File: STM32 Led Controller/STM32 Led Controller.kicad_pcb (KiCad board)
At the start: 2 copper layers, 1 part, among them U1 STM32G0B0RETx

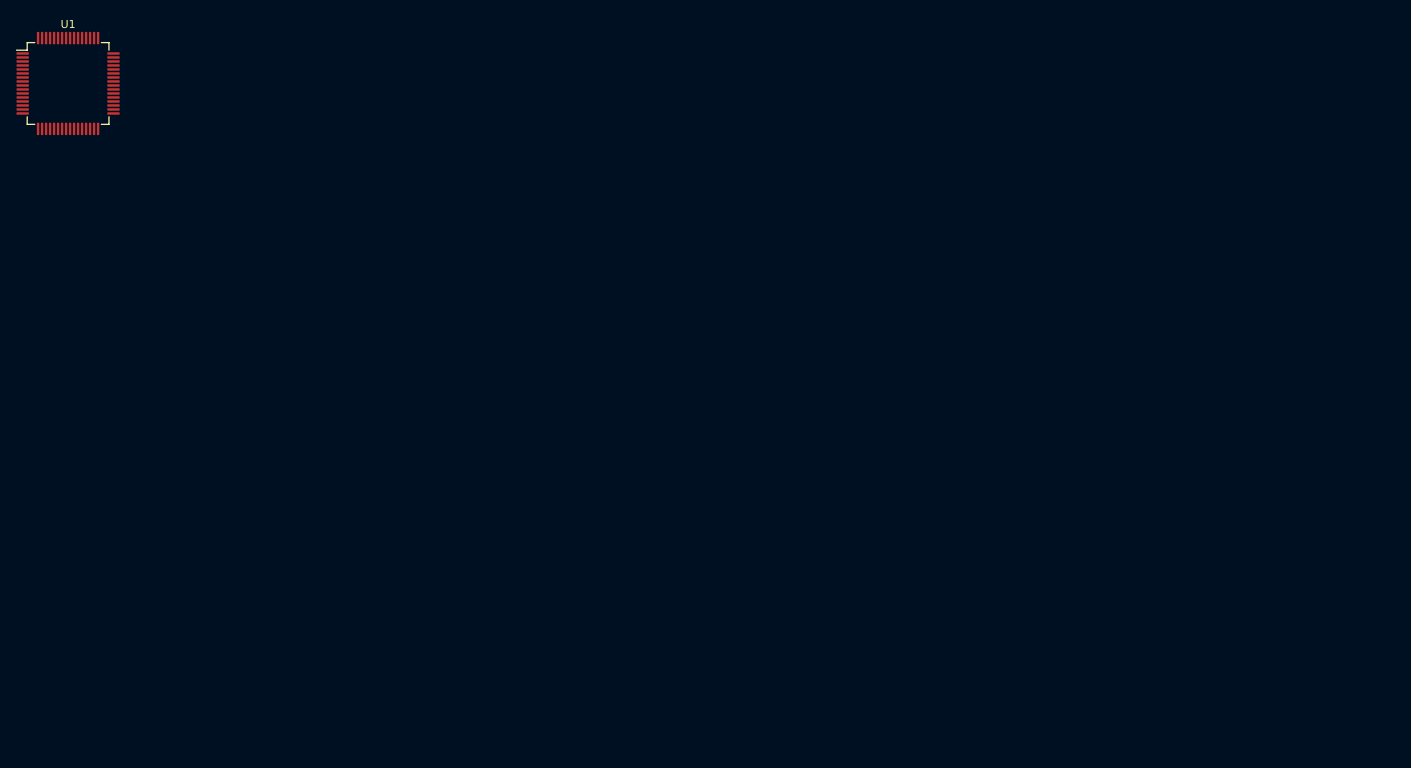
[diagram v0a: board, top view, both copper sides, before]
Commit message: Tweaked schematic Initial PCB layout/wiring (subject to change) Still need to add name/rev to silk screen
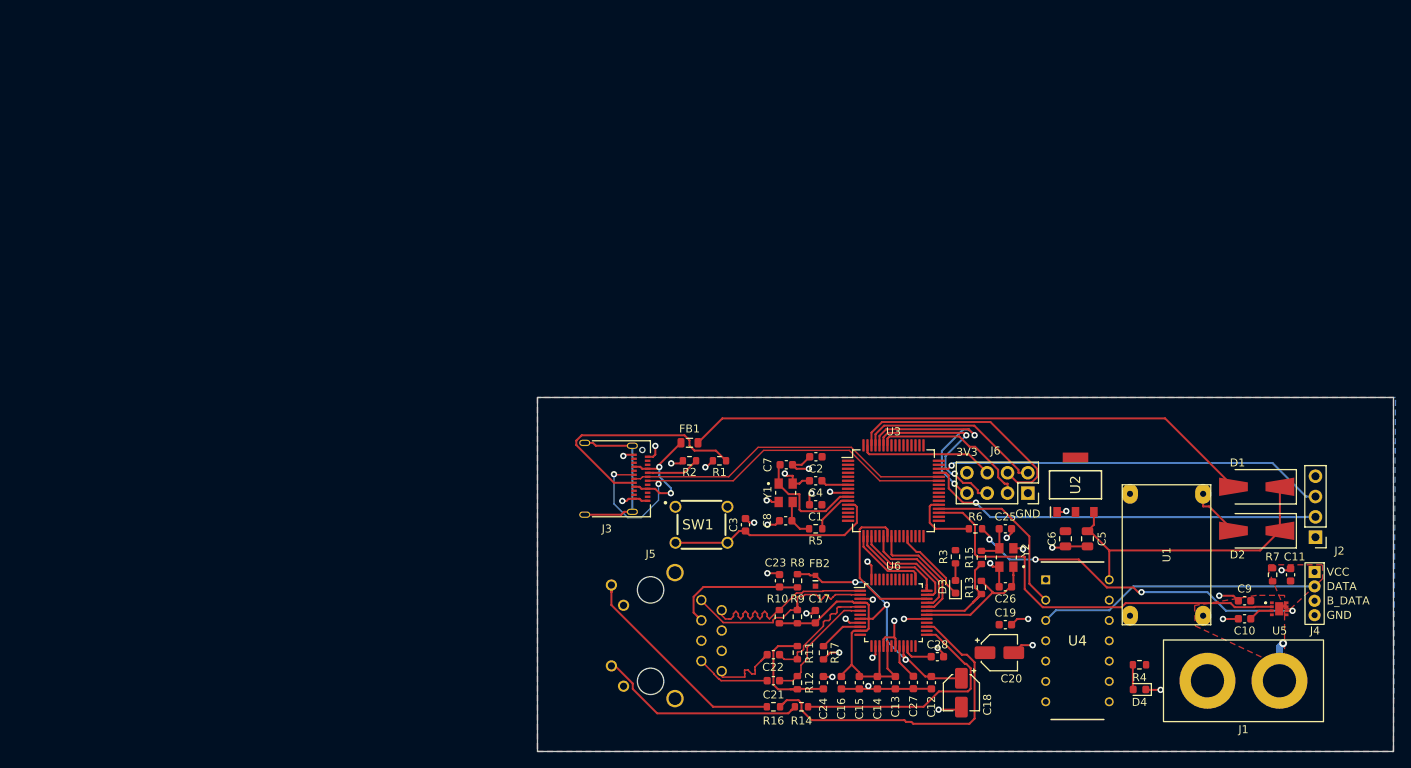
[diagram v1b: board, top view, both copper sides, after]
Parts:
- added C1: 0.1uF, Capacitor_SMD:C_0603_1608Metric, F.Cu at (149.8, 89.9)
- added C10: 1uF, Capacitor_SMD:C_0603_1608Metric, F.Cu at (203.4, 104.2)
- added C11: 0.1uF, Capacitor_SMD:C_0603_1608Metric, F.Cu at (209.1, 98.7)
- added C12: 0.1uF, Capacitor_SMD:C_0603_1608Metric, F.Cu at (164.2, 112.2)
- added C13: 0.1uF, Capacitor_SMD:C_0603_1608Metric, F.Cu at (159.7, 112.2)
- added C14: 0.1uF, Capacitor_SMD:C_0603_1608Metric, F.Cu at (157.5, 112.2)
- added C15: 0.1uF, Capacitor_SMD:C_0603_1608Metric, F.Cu at (155.2, 112.2)
- added C16: 0.1uF, Capacitor_SMD:C_0603_1608Metric, F.Cu at (153.0, 112.2)
- added C17: 0.1uF, Capacitor_SMD:C_0603_1608Metric, F.Cu at (149.7, 103.9)
- added C18: 10uF, Capacitor_SMD:CP_Elec_4x5.3, F.Cu at (168.0, 113.4)
- added C19: 0.1uF, Capacitor_SMD:C_0603_1608Metric, F.Cu at (173.5, 104.9)
- added C2: 4.7uF, Capacitor_SMD:C_0603_1608Metric, F.Cu at (149.8, 83.9)
- added C20: 10uF, Capacitor_SMD:CP_Elec_4x5.3, F.Cu at (172.7, 108.4)
- added C21: 6.8nF, Capacitor_SMD:C_0603_1608Metric, F.Cu at (144.5, 111.9)
- added C22: 6.8nF, Capacitor_SMD:C_0603_1608Metric, F.Cu at (144.5, 108.7)
- added C23: 0.1uF, Capacitor_SMD:C_0603_1608Metric, F.Cu at (145.2, 99.4)
- added C24: 10nF, Capacitor_SMD:C_0603_1608Metric, F.Cu at (150.7, 112.2)
- added C25: 30pF, Capacitor_SMD:C_0603_1608Metric, F.Cu at (173.5, 92.9)
- added C26: 30pF, Capacitor_SMD:C_0603_1608Metric, F.Cu at (173.5, 100.2)
- added C27: 4.7uF, Capacitor_SMD:C_0603_1608Metric, F.Cu at (162.0, 112.1)
- added C28: 10nF, Capacitor_SMD:C_0603_1608Metric, F.Cu at (165.0, 108.9)
- added C3: 0.1uF, Capacitor_SMD:C_0603_1608Metric, F.Cu at (141.0, 92.4)
- added C4: 0.1uF, Capacitor_SMD:C_0603_1608Metric, F.Cu at (149.8, 86.9)
- added C5: 10uF, Capacitor_SMD:C_0805_2012Metric, F.Cu at (183.8, 94.2)
- added C6: 10uF, Capacitor_SMD:C_0805_2012Metric, F.Cu at (181.0, 94.2)
- added C7: 30pF, Capacitor_SMD:C_0603_1608Metric, F.Cu at (146.1, 84.9)
- added C8: 30pF, Capacitor_SMD:C_0603_1608Metric, F.Cu at (146.0, 91.9)
- added C9: 1uF, Capacitor_SMD:C_0603_1608Metric, F.Cu at (203.4, 101.9)
- added D1: D_Schottky, Diode_SMD:D_SMA-SMB_Universal_Handsoldering, F.Cu at (204.9, 87.7)
- added D2: D_Schottky, Diode_SMD:D_SMA-SMB_Universal_Handsoldering, F.Cu at (204.9, 93.2)
- added D3: LED, LED_SMD:LED_0603_1608Metric, F.Cu at (167.2, 100.2)
- added D4: LED, LED_SMD:LED_0603_1608Metric, F.Cu at (190.2, 113.0)
- added FB1: 100R, Inductor_SMD:L_0805_2012Metric, F.Cu at (134.0, 82.2)
- added FB2: BLM18PG121SN1D, SamacSys_Parts:BLM18SP221SN1B, F.Cu at (149.8, 99.4)
- added J1: EXT_PWR_CONN, Custom Connectors:1x02 M4 RING, F.Cu at (203.2, 111.9)
- added J2: SWD_CONN, Connector_PinHeader_2.54mm:PinHeader_1x04_P2.54mm_Vertical, F.Cu at (212.2, 94.0)
- added J3: USB_C_Receptacle_USB2.0_16P, Connector_USB:USB_C_Receptacle_Amphenol_12401610E4-2A, F.Cu at (123.8, 86.7)
- added J4: WS2815, Custom Connectors:LED Strip Connector, F.Cu at (212.2, 101.0)
- added J5: RB1-125BAG1A, RB1-125BAG1A:WIZNET_RB1-125BAG1A, F.Cu at (129.1, 106.3)
- added J6: Conn_02x04_Top_Bottom, Connector_PinSocket_2.54mm:PinSocket_2x04_P2.54mm_Vertical, F.Cu at (176.3, 88.5)
- added R1: 5.11K, Resistor_SMD:R_0603_1608Metric, F.Cu at (137.8, 84.4)
- added R10: 49.9, Resistor_SMD:R_0603_1608Metric, F.Cu at (145.2, 103.9)
- added R11: 49.9, Resistor_SMD:R_0603_1608Metric, F.Cu at (147.5, 108.4)
- added R12: 49.9, Resistor_SMD:R_0603_1608Metric, F.Cu at (147.5, 112.2)
- added R13: 1M, Resistor_SMD:R_0603_1608Metric, F.Cu at (170.5, 100.3)
- added R14: 220, Resistor_SMD:R_0603_1608Metric, F.Cu at (148.0, 115.2)
- added R15: 330, Resistor_SMD:R_0603_1608Metric, F.Cu at (170.5, 96.5)
- added R16: 220, Resistor_SMD:R_0603_1608Metric, F.Cu at (144.5, 115.2)
- added R17: 12.4K, Resistor_SMD:R_0603_1608Metric, F.Cu at (150.8, 108.4)
- added R2: 5.11K, Resistor_SMD:R_0603_1608Metric, F.Cu at (134.0, 84.4)
- added R3: 100K, Resistor_SMD:R_0603_1608Metric, F.Cu at (167.2, 96.4)
- added R4: 100K, Resistor_SMD:R_0603_1608Metric, F.Cu at (190.2, 109.9)
- added R5: 330, Resistor_SMD:R_0603_1608Metric, F.Cu at (149.8, 92.9)
- added R6: 100K, Resistor_SMD:R_0603_1608Metric, F.Cu at (169.8, 92.9)
- added R7: 100, Resistor_SMD:R_0603_1608Metric, F.Cu at (206.9, 98.7)
- added R8: 10, Resistor_SMD:R_0603_1608Metric, F.Cu at (147.5, 99.4)
- added R9: 49.9, Resistor_SMD:R_0603_1608Metric, F.Cu at (147.5, 103.9)
- added SW1: FSM4JH, SamacSys_Parts:FSM4JH, F.Cu at (135.5, 92.4)
- added U2: NCV1117ST33T3G, SamacSys_Parts:SOT230P700X180-4N, F.Cu at (182.2, 87.4)
- added U3: STM32G0B0RETx, Package_QFP:LQFP-64_10x10mm_P0.5mm, F.Cu at (159.5, 88.2)
- added U4: SN74AHCT125N, SamacSys_Parts:DIP794W53P254L1930H508Q14N, F.Cu at (182.5, 106.9)
- added U5: DML3006LFDS-7, SamacSys_Parts:DML3006LFDS7, F.Cu at (207.7, 102.9)
- added U6: W5500, Package_QFP:LQFP-48_7x7mm_P0.5mm, F.Cu at (159.5, 103.4)
- added Y1: ABM8-48.000MHZ-B2-T, SnapEDA Library:XTAL_ABM8-48.000MHZ-B2-T, F.Cu at (146.0, 88.4)
- added Y2: ABM8-25.000MHZ-B2-T, SnapEDA Library:XTAL_ABM8-48.000MHZ-B2-T, F.Cu at (173.6, 96.5)
- U1: value STM32G0B0RETx -> Mini360; footprint Package_QFP:LQFP-64_10x10mm_P0.5mm -> Mini360_step-down:Mini360_step-down
- moved U1 149.4 mm to (193.6, 96.2), turned to 90 degrees
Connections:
- U1 pad 1: unconnected-(U1-PC11-Pad1) -> GND
- U1 pad 2: unconnected-(U1-PC12-Pad2) -> +12V
- U1 pad 3: unconnected-(U1-PC13-Pad3) -> GND
- U1 pad 4: unconnected-(U1-PC14-Pad4) -> Net-(D2-A)
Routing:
- net GND: track 0.00 -> 91.0 mm, vias 0 -> 36
- net +3.3VA: track 0.00 -> 73.6 mm, vias 0 -> 3
- net Net-(D1-A): track 0.00 -> 71.7 mm
- net USB_D-: track 0.00 -> 55.4 mm, vias 0 -> 2
- net LED_PWR_EN: track 0.00 -> 51.5 mm
- net STM_SWDIO: track 0.00 -> 50.3 mm, vias 0 -> 1
- net STM_SWCLK: track 0.00 -> 49.1 mm, vias 0 -> 1
- net Net-(U5-PG): track 0.00 -> 44.0 mm, vias 0 -> 4
- net Net-(U6-ACTLED): track 0.00 -> 42.1 mm
- net USB_D+: track 0.00 -> 41.3 mm
- net +5V: track 0.00 -> 38.0 mm
- net LED_DATA_5V: track 0.00 -> 35.4 mm
- net Net-(U6-LINKLED): track 0.00 -> 31.0 mm
- net ESP_EN: track 0.00 -> 30.8 mm
- net Net-(J3-CC2): track 0.00 -> 30.4 mm
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- added copper zone on F.Cu, net +12V
- added copper zone on F.Cu, net +3V3
- added copper zone on B.Cu, net GND
- added copper zone on F.Cu, net VDD
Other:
- board outline added: 107 x 44.2 mm
